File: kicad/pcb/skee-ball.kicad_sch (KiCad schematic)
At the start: 68 parts, among them J13 HEADER, J18 DC_DRIVER, J19 JOYSTICK, J2 EXTERNAL_BUTTON, J20 SERVO, J21 US0, J22 US1, J26 US2, J27 US3, J3 NHD_CONN1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

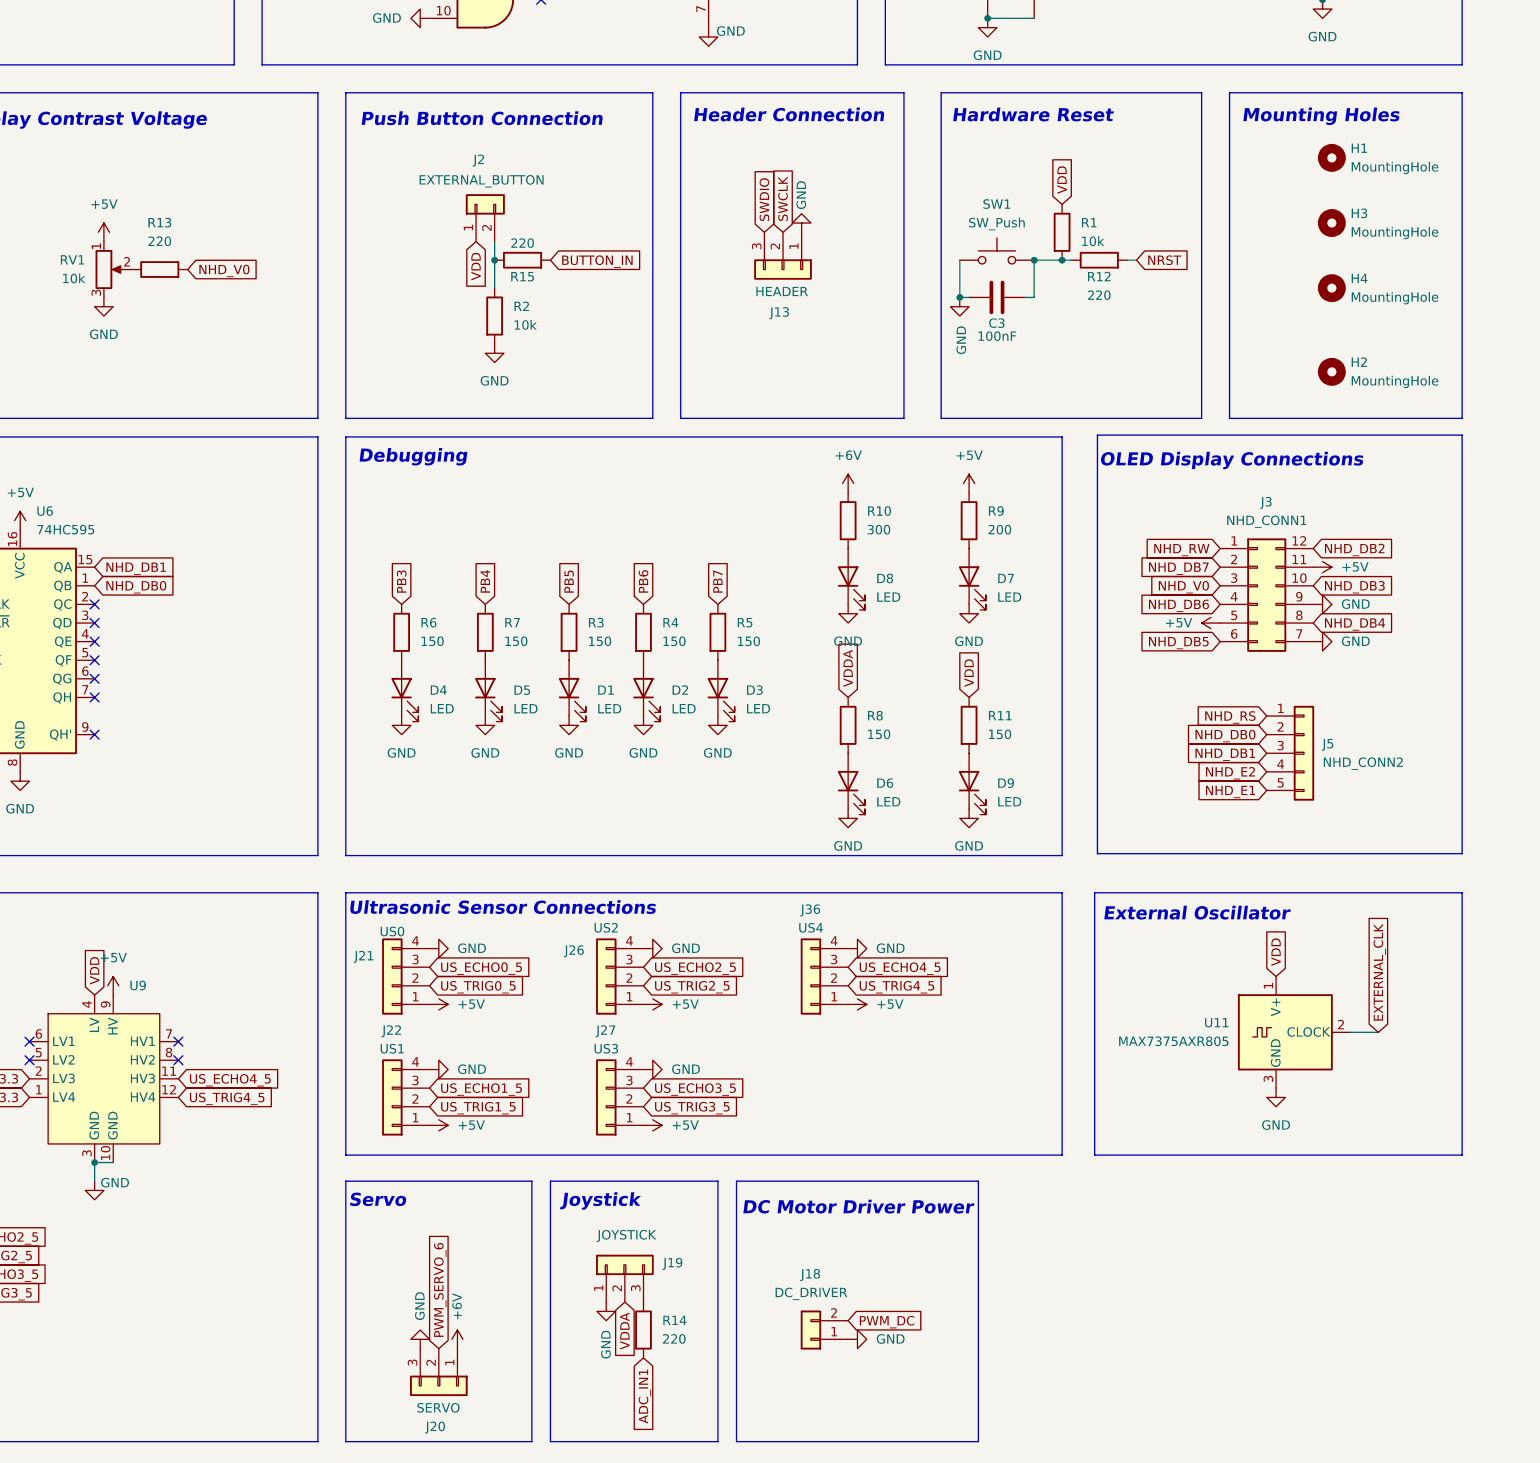
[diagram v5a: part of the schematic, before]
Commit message: add esd protection diodes
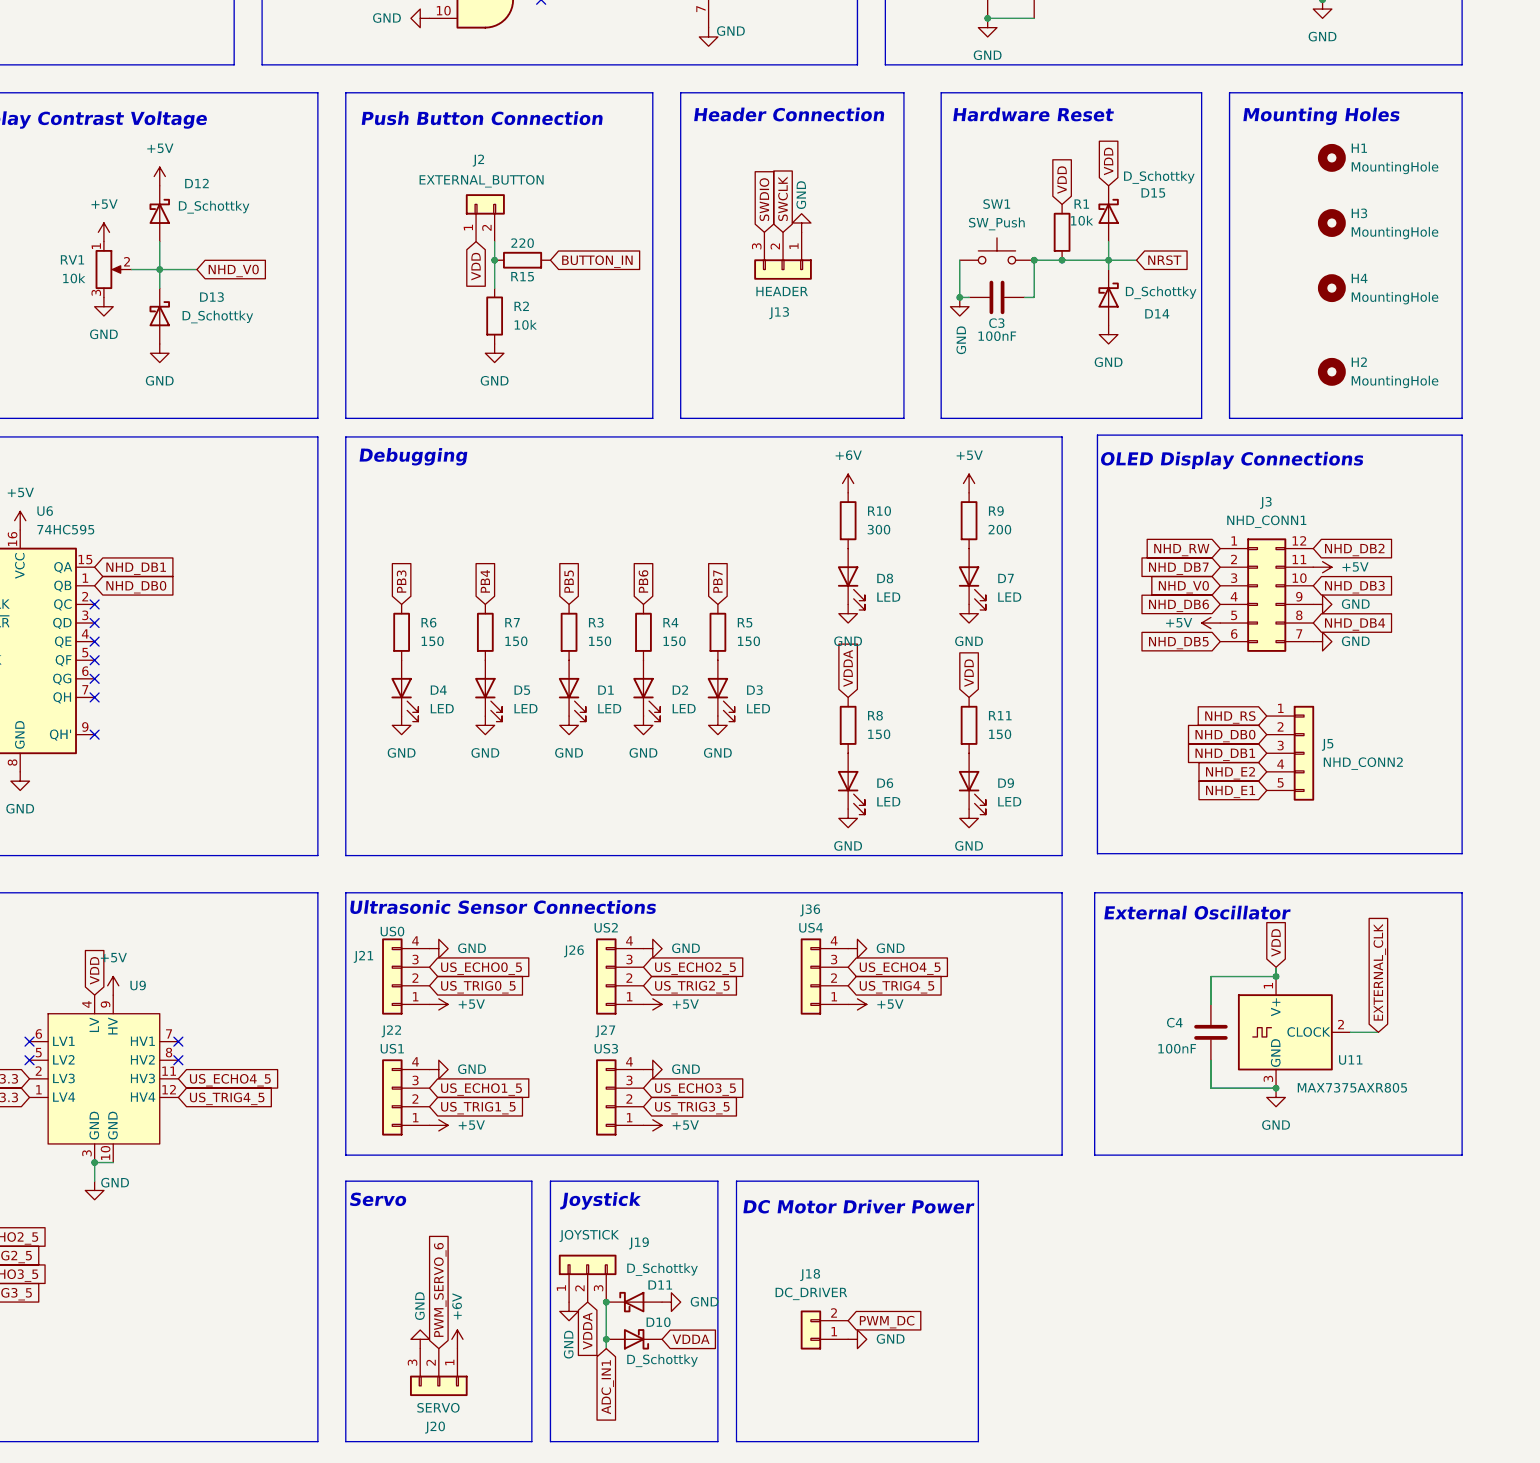
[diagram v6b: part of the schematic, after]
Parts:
- removed R12, R13, R14: 220, Resistor_SMD:R_0805_2012Metric_Pad1.20x1.40mm_HandSolder, symbol Device:R
- added C4: 100nF, Capacitor_SMD:C_0805_2012Metric_Pad1.18x1.45mm_HandSolder, symbol Device:C
- added D10, D11, D12, D13, D14, D15: D_Schottky, Diode_SMD:D_0805_2012Metric, symbol Device:D_Schottky
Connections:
- net +5V: now also D12.1 (K)
- net ADC_IN1: now also J19.3 (Pin_3), D10.2 (A), D11.1 (K)
- net GND: now also C4.2, D11.2 (A), D13.2 (A), D14.2 (A)
- net NHD_V0: now also RV1.2, D12.2 (A), D13.1 (K)
- net NRST: now also C3.2, R1.2, SW1.2, D14.1 (K), D15.2 (A)
- net VDD: now also C4.1, D15.1 (K)
- net VDDA: now also D10.1 (K)
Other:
- moved on the sheet: J19
